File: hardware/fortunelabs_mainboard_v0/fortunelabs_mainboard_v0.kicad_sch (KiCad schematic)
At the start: 94 parts, among them J1 Conn_02x16_Odd_Even, J2 Conn_02x16_Odd_Even, J3 USB_C_Receptacle_USB2.0_14P, J4 Micro_SD_Card_Det_Hirose_DM3AT, J5 Conn_02x07_Odd_Even, Q1 AO3401A, SW1 BOOT, SW2 RESET, U1 ADS1115, U2 MCP23017_ML, U3 ESP32-S3-WROOM-2, U4 ADS1115, U5 TPS62162DSG, U6 DS3232M, U7 TPL5010, U8 ULN2803A

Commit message: hw(hardware): renumber R/C designators into per-block hundred bands
Passive designators had accumulated in drawing order, not functional
order: the ADS1115 block owned R1-R7 and C1-C5 because it was drawn
first, power management landed at R16/R17, and the SD card block was
split across R23 and R41-R44 as parts were tacked on. No block owned a
contiguous range, so a designator carried no information about where it
sat on the board.

Each block now owns a hundred band, ordered power first, then MCU, then
peripherals outward:

  1xx  power management        R101-R102   C101-C103
  2xx  ESP32-S3 MCU            R201        C201-C203
  3xx  USB-C interface         R301-R302
  4xx  SPI SD card             R401-R405   C401-C402
  5xx  realtime clock          R501        C501
  6xx  watchdog                R601-R602   C601
  7xx  MCP23017 GPIO expander  R701-R703   C701
  8xx  ADS1115 analog input    R801-R812   C801-C810
  9xx  output driver array     R901-R916

Existing relative order is preserved within each block. The ADS1115
channel resistors and the two output banks (DNP, then 470R) were already
in a deliberate sequence; re-sorting by sheet position would have
scrambled it. The two on-sheet annotation labels naming ranges were
updated to match. Symbol positions were tuned by hand afterwards for
readability.

Done now because the PCB carries no footprints yet, so there is no
layout to re-link. The cost of this change only goes up from here.

The generated BOM is left untouched. It drifted several commits ago and
re-exporting it here would pull that unrelated drift into a hardware
commit.

ERC: 0 violations.
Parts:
- renumbered C12 to C101, C13 to C102, C14 to C103, C18 to C201, C19 to C202, C20 to C203, C15 to C401, C16 to C402, C17 to C501, C21 to C601, C6 to C701, C1 to C801, C2 to C802, C3 to C803, C4 to C804, C5 to C805, C7 to C806, C8 to C807, C9 to C808, C10 to C809, C11 to C810, R16 to R101, R17 to R102, R24 to R201, R18 to R301, R19 to R302, R23 to R401, R41 to R402, R42 to R403, R43 to R404, R44 to R405, R20 to R501, R21 to R601, R22 to R602, R8 to R701, R9 to R702, R10 to R703, R1 to R801, R2 to R802, R3 to R803, R4 to R804, R5 to R805, R6 to R806, R7 to R807, R11 to R808, R12 to R809, R13 to R810, R14 to R811, R15 to R812, R25 to R901, R26 to R902, R27 to R903, R28 to R904, R29 to R905, R30 to R906, R31 to R907, R32 to R908, R33 to R909, R34 to R910, R35 to R911, R36 to R912, R37 to R913, R38 to R914, R39 to R915, R40 to R916
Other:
- note added: "R901-R908 DNP"
- note added: "R909-R916 470"
- note removed: "R25-R32 DNP"
- note removed: "R33-R40 470"

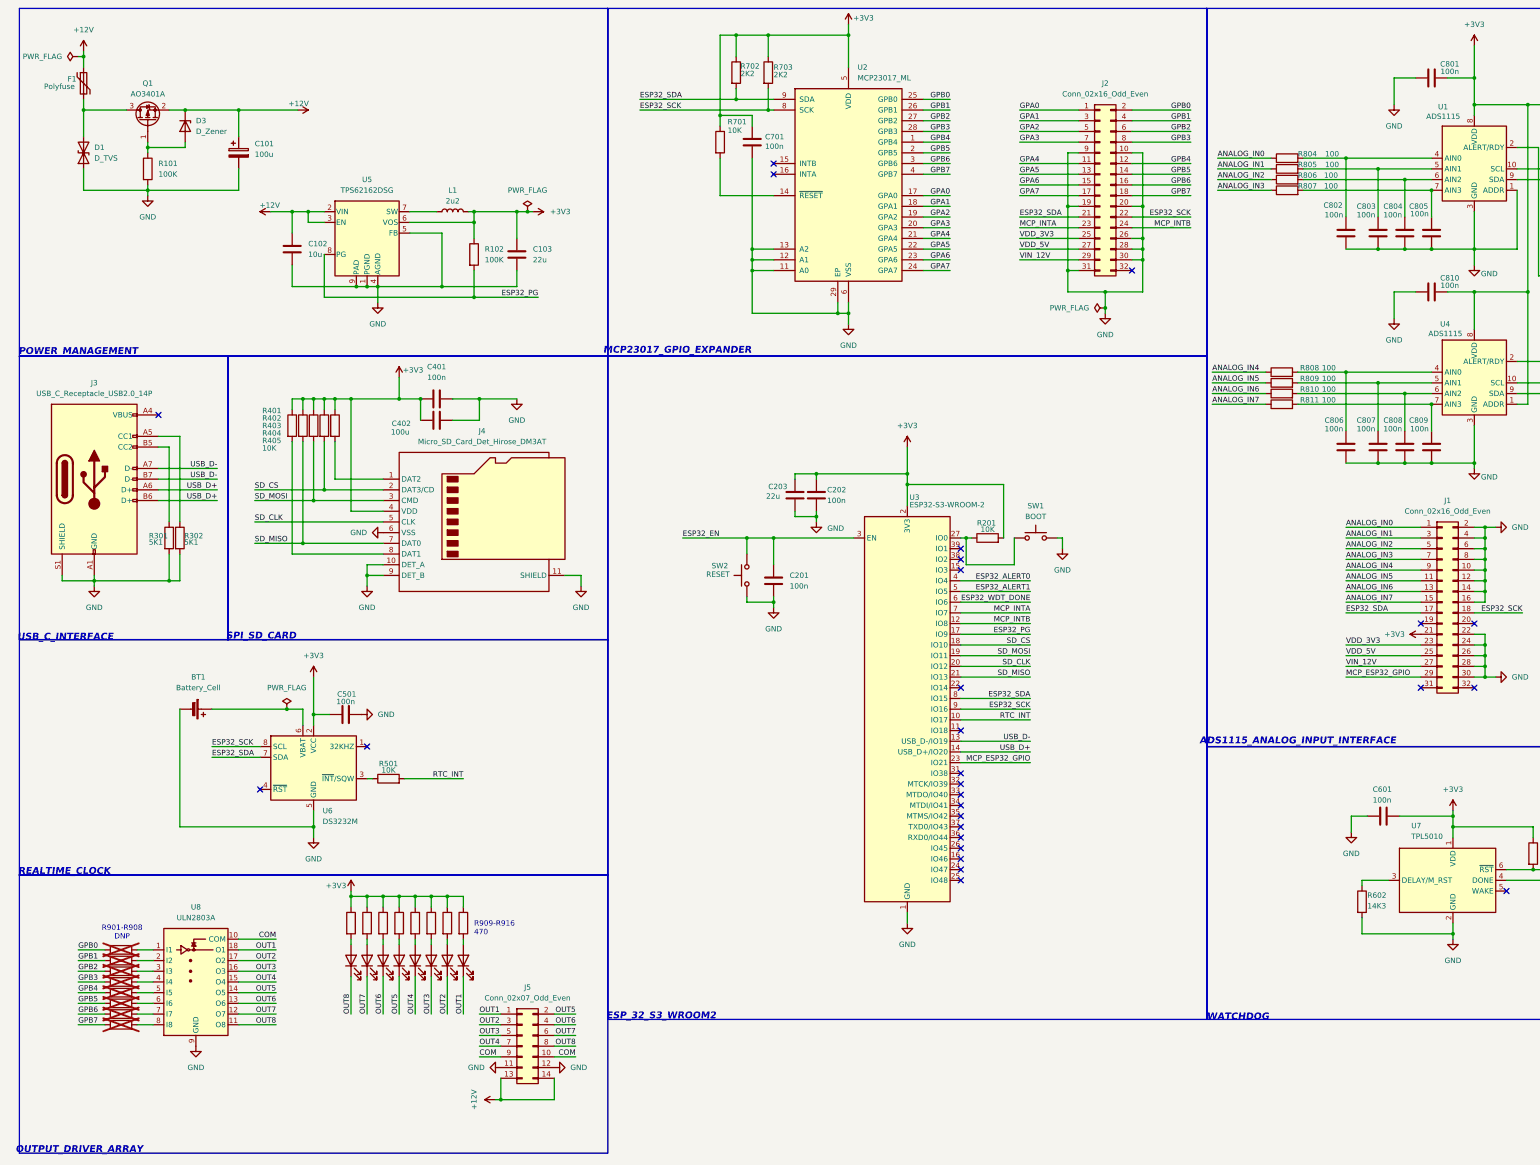
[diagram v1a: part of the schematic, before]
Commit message: hw(hardware): extend designator bands to all classes, add inlet, indicators and test points
Completes the scheme started for R/C in 6c715c6. D, F, L, Q, U, SW and J now
carry the same per-block hundred band:

  1xx power       D101-D104 F101 J101 L101 Q101 U101
  2xx MCU         SW101 SW102 U201
  3xx USB-C       J301
  4xx SD card     J401
  5xx RTC         U501
  6xx watchdog    U601
  7xx GPIO exp    J701 U701
  8xx analog in   J801 U801 U802
  9xx output      D901-D908 J901 U901

U801/U802 is the point of the exercise: the two ADS1115 were U1 and U4, which
actively hid that they are the same part twice.

Test points stay flat, TP1-TP9. This is deliberate and is not an oversight to be
tidied later. A test point is probed by hand against a printed list, not traced
through a block on the sheet, so a short number is worth more at the bench than a
number that encodes provenance.

New parts:

  J101         barrel jack. +12V has had no inlet; J901.13/14 is a rail tap for
               field wiring, not a supply. Closes the gap noted in #37
  D103 + R103  12V present indicator, 10K, 1.0 mA
  D104 + R104  3V3 present indicator, 2K2, 0.59 mA
  TP1 SDA      TP2 SCL      TP3 +12V     TP4 +12V     TP5 +3V3
  TP6 GND      TP7 PG       TP8 EN       TP9 WDT_DONE

The indicator resistors are sized so the two rails read at comparable brightness.
The dark-3V3 case is the one worth seeing, because 12V present with 3V3 dead is
the failure that points at the regulator, and an indicator pair that cannot be
compared by eye does not report it.

TP3 and TP4 both land on +12V today because the protected rail does not exist
yet. They separate when #37 splits the node; placing them now is what makes the
straddle measurement possible without a second spin.

Every symbol carries a footprint, which is the standing requirement in #27.

This commit bundles two hardware changes, against the one-per-commit rule. The
GUI edits interleaved, and splitting them afterwards would mean writing out an
i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
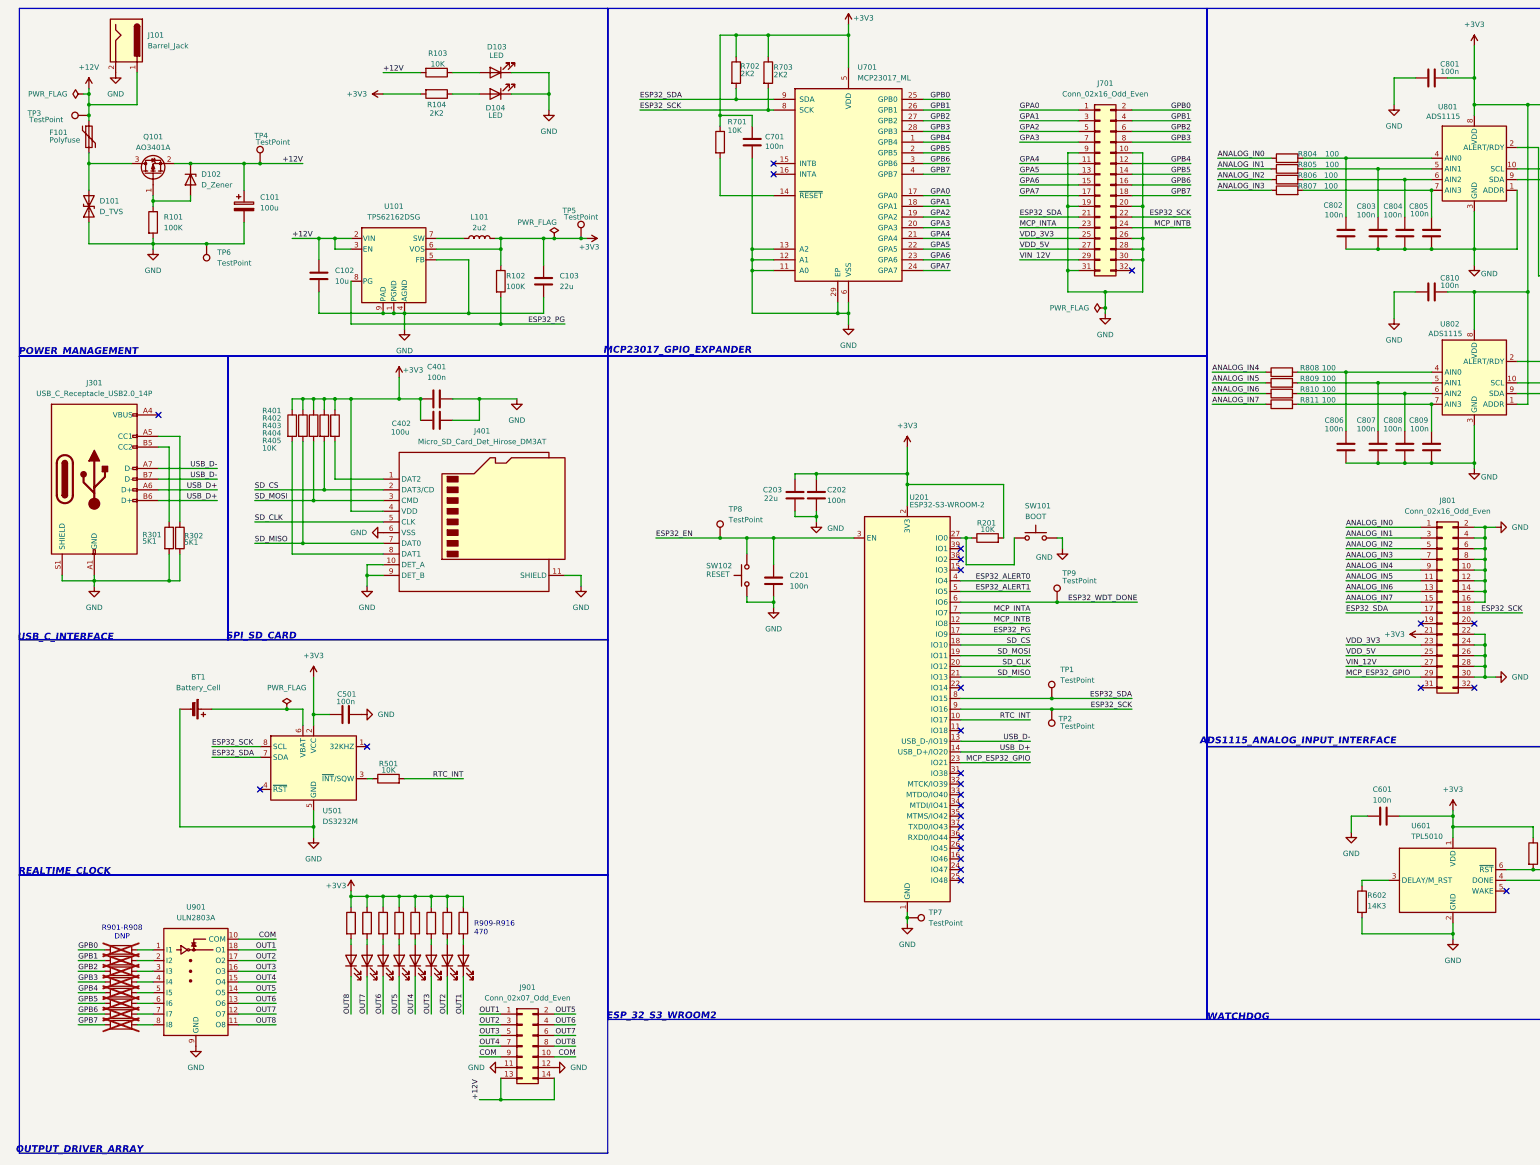
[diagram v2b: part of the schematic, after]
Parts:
- added D103, D104: LED, LED_SMD:LED_0603_1608Metric, symbol Device:LED
- added J101: Barrel_Jack, Connector_BarrelJack:BarrelJack_CUI_PJ-063AH_Horizontal, symbol Connector:Barrel_Jack
- added R103: 10K, Resistor_SMD:R_0603_1608Metric, symbol Device:R
- added R104: 2K2, Resistor_SMD:R_0603_1608Metric, symbol Device:R
- added TP1, TP2, TP3, TP4, TP5, TP8, TP9: TestPoint, TestPoint:TestPoint_Plated_Hole_D2.0mm, symbol Connector:TestPoint
- added TP6, TP7: TestPoint, TestPoint:TestPoint_Loop_D2.50mm_Drill1.0mm_LowProfile, symbol Connector:TestPoint
- renumbered D1 to D101, D3 to D102, D2 to D901, D4 to D902, D5 to D903, D6 to D904, D7 to D905, D8 to D906, D9 to D907, D10 to D908, F1 to F101, J3 to J301, J4 to J401, J2 to J701, J1 to J801, J5 to J901, L1 to L101, Q1 to Q101, SW1 to SW101, SW2 to SW102, U5 to U101, U3 to U201, U6 to U501, U7 to U601, U2 to U701, U1 to U801, U4 to U802, U8 to U901
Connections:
- net +12V: now also J101.1, R103.2, TP3.1, TP4.1
- net +3V3: now also R104.2, TP5.1
- net ESP32_EN: now also TP8.1
- net ESP32_SCK: now also TP2.1
- net ESP32_SDA: now also TP1.1
- net ESP32_WDT_DONE: now also TP9.1
- net GND: now also D103.1 (K), D104.1 (K), J101.2, TP6.1, TP7.1
- new net: D103.2 (A), R103.1
- new net: D104.2 (A), R104.1
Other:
- moved on the sheet: C101, C102, C103, D101, D102, F101, L101, Q101, R101, R102, U101

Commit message: hw(hardware): connect MCP23017 INTA/INTB to the ESP32
U701 pins 15 and 16 carried explicit no_connect markers. The interrupt
outputs went nowhere, so the expander could not signal a pin change and the
ESP32 would have had to poll it over I2C.

The nets existed and looked right. MCP_INTA and MCP_INTB ran from U201 IO7
and IO8 to J701.23/24, so the sheet showed named interrupt lines the whole
time; they simply never reached the chip they were named for. The
no_connect markers are why ERC stayed quiet, a marked pin being one ERC has
been told to ignore.

  MCP_INTA   U201.7  <-> J701.23  <-> U701.16
  MCP_INTB   U201.12 <-> J701.24  <-> U701.15

Two separate GPIOs, not the wire-OR the task list asks for in 4.2. Two lines
tell the ESP32 which port fired without a register read to find out. The
task list still specifies wire-OR open-drain and now disagrees with the
board; that is a spec change and does not belong in this commit.

No pull-ups, and so no BOM change. IOCON.ODR defaults to 0, which leaves the
INT pins as active drivers. Pull-ups would only be needed for the open-drain
wire-OR arrangement.

The two new wires cross the verticals at x=186.69 and x=179.07 without
junctions. Crossing is not connection: the netlist export confirms both nets
carry three nodes each and nothing else.

ERC: 0 violations.
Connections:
- net MCP_INTA: now also U701.16 (INTA)
- net MCP_INTB: now also U701.15 (INTB)
- no-connect marks 27 -> 25
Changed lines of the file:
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@@
 	)
 	(no_connect
-		(at 191.77 49.53)
-	)
-	(no_connect
 		(at 95.25 187.96)
 	)
@@
 	)
 	(no_connect
-		(at 191.77 52.07)
-	)
-	(no_connect
 		(at 236.22 140.97)
 	)
@@
 	(wire
 		(pts
+			(xy 165.1 52.07) (xy 191.77 52.07)
+		)
+		(stroke
+			(width 0)
+			(type default)
+		)
+	)
+	(wire
+		(pts
 			(xy 236.22 148.59) (xy 252.73 148.59)
 		)
@@
 	(wire
 		(pts
+			(xy 165.1 49.53) (xy 191.77 49.53)
+		)
+		(stroke
+			(width 0)
+			(type default)
+		)
+	)
+	(wire
+		(pts
 			(xy 387.35 73.66) (xy 406.4 73.66)
 		)
@@
 		)
 	)
+	(label "MCP_INTB"
+		(at 165.1 49.53 0)
+		(effects
+			(font
+				(size 1.27 1.27)
+			)
+			(justify left bottom)
+		)
+	)
 	(label "GPA1"
 		(at 250.19 39.37 0)
@@
 		(effects
 			(font
+				(size 1.27 1.27)
+			)
+			(justify left bottom)
+		)
+	)
+	(label "MCP_INTA"
+		(at 165.1 52.07 0)
+		(effects
+			(font

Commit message: hw(hardware): add the heartbeat LED on IO48
D201 with R202 (2K2) in series, anode to the resistor and cathode to
GND, driven from U201 pin 25 (IO48) on the net LED_HEART. Active high:
the MCU sources the current.

IO48 carries no strapping function on the ESP32-S3 and is Espressif's
own convention for a module status LED, so a probe there means the same
thing on this board as on a devkit. It was unconnected before this.

This is the only indicator the MCU can drive without the I2C bus. The
D901-D908 bank sits behind the ULN2803A and the MCP23017, so it cannot
light before the bus is up and cannot report a fault in the I2C path
itself. 2K2 gives roughly 0.6 mA at 3V3: dim, visible, and far inside
the per-pin budget.

Designators follow the block bands, 2xx being the MCU block. R201 was
already taken by the IO0 pull-up.
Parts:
- added D201: LED_HEART, LED_SMD:LED_0603_1608Metric, symbol Device:LED
- added R202: 2K2, Resistor_SMD:R_0603_1608Metric, symbol Device:R
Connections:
- net GND: now also D201.1 (K)
- net at U201.25 (IO48): now also R202.1
- new net: D201.2 (A), R202.2
- no-connect marks 25 -> 24
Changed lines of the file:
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@@
 	)
 	(no_connect
-		(at 236.22 219.71)
-	)
-	(no_connect
 		(at 236.22 184.15)
 	)
@@
 	(wire
 		(pts
+			(xy 264.16 219.71) (xy 264.16 223.52)
+		)
+		(stroke
+			(width 0)
+			(type default)
+		)
+	)
+	(wire
+		(pts
 			(xy 182.88 34.29) (xy 191.77 34.29)
 		)
@@
 	(wire
 		(pts
+			(xy 259.08 219.71) (xy 264.16 219.71)
+		)
+		(stroke
+			(width 0)
+			(type default)
+		)
+	)
+	(wire
+		(pts
+			(xy 236.22 219.71) (xy 240.03 219.71)
+		)
+		(stroke
+			(width 0)
+			(type default)
+		)
+	)
+	(wire
+		(pts
 			(xy 99.06 85.09) (xy 101.6 85.09)
 		)
@@
 	(wire
 		(pts
+			(xy 247.65 219.71) (xy 251.46 219.71)
+		)
+		(stroke
+			(width 0)
+			(type default)
+		)
+	)
+	(wire
+		(pts
 			(xy 64.77 246.38) (xy 73.66 246.38)
 		)
@@
 	)
 	(symbol
+		(lib_id "Device:R")
+		(at 243.84 219.71 90)
+		(unit 1)
+		(exclude_from_sim no)
+		(in_bom yes)
+		(on_board yes)
+		(dnp no)
+		(property "Reference" "R202"
+			(at 243.84 214.884 90)
+			(effects
+				(font
+					(size 1.27 1.27)
+				)
+			)
+		)
+		(property "Value" "2K2"
+			(at 243.84 217.424 90)
+			(effects
+				(font
+					(size 1.27 1.27)
+				)
+			)
+		)
+		(property "Footprint" "Resistor_SMD:R_0603_1608Metric"
+			(at 243.84 221.488 90)
+			(effects
+				(font
+					(size 1.27 1.27)
+				)
+				(hide yes)
+			)
+		)
+		(property "Datasheet" "~"
+			(at 243.84 219.71 0)
+			(effects
+				(font
+					(size 1.27 1.27)
+				)
+				(hide yes)
+			)
+		)
+		(property "Description" "Resistor"
+			(at 243.84 219.71 0)
+			(effects
+				(font
+					(size 1.27 1.27)
+				)
+				(hide yes)
+			)
+		)
+		(pin "1"
+		)
+		(pin "2"
+		)
+		(instances
+			(project "fortunelabs_mainboard_v0"
+				(path "/1727eecb-65c8-4b57-aa8a-814f366e0831"
+					(reference "R202")
+					(unit 1)
+				)
+			)
+		)
+	)
+	(symbol
 		(lib_id "Device:LED")
 		(at 114.3 238.76 90)
@@
 	)
 	(symbol
+		(lib_id "power:GND")
+		(at 264.16 223.52 0)
+		(unit 1)
+		(exclude_from_sim no)
+		(in_bom yes)
+		(on_board yes)
+		(dnp no)
+		(fields_autoplaced yes)
+		(property "Reference" "#PWR031"
+			(at 264.16 229.87 0)
+			(effects
+				(font
+					(size 1.27 1.27)
+				)
+				(hide yes)
+			)
+		)
+		(property "Value" "GND"
+			(at 264.16 228.6 0)
+			(effects
+				(font
+					(size 1.27 1.27)
+				)
+			)
+		)
+		(property "Footprint" ""
+			(at 264.16 223.52 0)
+			(effects
+				(font
+					(size 1.27 1.27)
+				)
+				(hide yes)
+			)
+		)
+		(property "Datasheet" ""
+			(at 264.16 223.52 0)
+			(effects
+				(font
+					(size 1.27 1.27)
+				)
+				(hide yes)
+			)
+		)
+		(property "Description" "Power symbol creates a global label with name \"GND\" , ground"
+			(at 264.16 223.52 0)
+			(effects
+				(font
+					(size 1.27 1.27)
+				)
+				(hide yes)
+			)
+		)
+		(pin "1"
+		)
+		(instances
+			(project "fortunelabs_mainboard_v0"
+				(path "/1727eecb-65c8-4b57-aa8a-814f366e0831"
+					(reference "#PWR031")
+					(unit 1)
+				)
+			)
+		)
+	)
+	(symbol
 		(lib_id "power:PWR_FLAG")
 		(at 139.7 67.31 0)
@@
 					(unit 1)
 				)
+			)
+		)
+	)
+	(symbol
+		(lib_id "Device:LED")
+		(at 255.27 219.71 180)
+		(unit 1)
+		(exclude_from_sim no)
+		(in_bom yes)
+		(on_board yes)
+		(dnp no)
+		(property "Reference" "D201"
+			(at 257.048 213.614 0)
+			(effects
+				(font
+					(size 1.27 1.27)
+				)
+			)
+		)
+		(property "Value" "LED_HEART"
+			(at 257.048 216.154 0)
+			(effects
+				(font
+					(size 1.27 1.27)
+				)
+			)
+		)
+		(property "Footprint" "LED_SMD:LED_0603_1608Metric"
+			(at 255.27 219.71 0)
+			(effects
+				(font
+					(size 1.27 1.27)
+				)
+				(hide yes)
+			)
+		)
+		(property "Datasheet" "~"
+			(at 255.27 219.71 0)
+			(effects
+				(font
+					(size 1.27 1.27)
+				)
+				(hide yes)
+			)
+		)
+		(property "Description" "Light emitting diode"
+			(at 255.27 219.71 0)
+			(effects
+				(font
+					(size 1.27 1.27)
+				)
+				(hide yes)
+			)
+		)
+		(property "Sim.Pins" "1=K 2=A"
+			(at 255.27 219.71 0)
+			(effects
+				(font
+					(size 1.27 1.27)
+				)
+				(hide yes)
+			)
+		)
+		(pin "1"
+		)
+		(pin "2"
+		)
+		(instances
+			(project "fortunelabs_mainboard_v0"
+				(path "/1727eecb-65c8-4b57-aa8a-814f366e0831"
+					(reference "D201")
+					(unit 1)
+				)

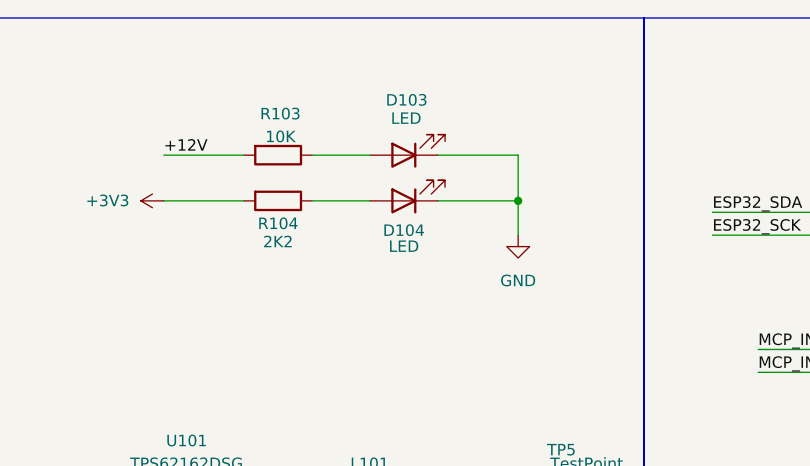
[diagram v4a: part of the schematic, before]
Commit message: hw(hardware): name the power indicators by the rail they watch
D103 becomes LED_12V and D104 becomes LED_3V3, from a shared Value of
LED. Both sit in the power block and each one reports a different rail,
which the schematic could not tell you before: the reader had to trace
the anode back to find out which supply an unlit LED was accusing.

Value is a grouping field in the BOM settings, so this also splits the
two of them out of the ten-part LED row. That is a presentation change
only. No net, footprint or fitment changes, and nothing here alters the
board.
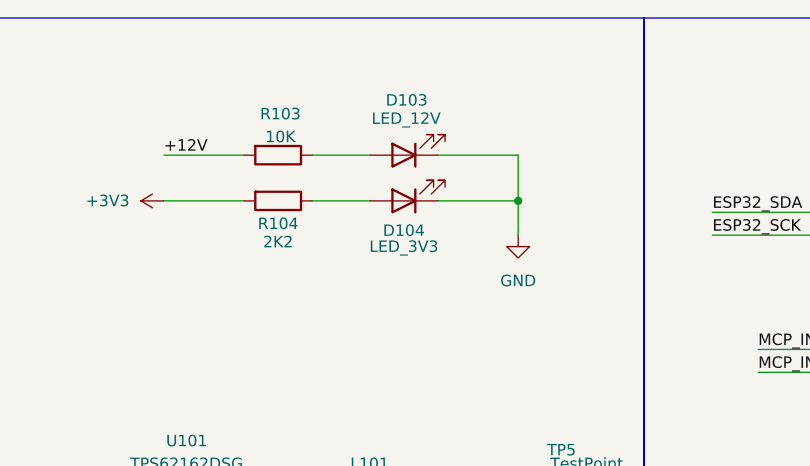
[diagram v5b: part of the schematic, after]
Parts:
- D103: value LED -> LED_12V
- D104: value LED -> LED_3V3
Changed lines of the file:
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@@
 			)
 		)
-		(property "Value" "LED"
+		(property "Value" "LED_12V"
 			(at 125.984 23.876 0)
 			(effects
@@
 			)
 		)
-		(property "Value" "LED"
+		(property "Value" "LED_3V3"
 			(at 125.73 38.1 0)
 			(effects
